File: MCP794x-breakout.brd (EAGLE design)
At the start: 22.8 x 15.2 mm, 11 parts, among them U4 MCP794x, X3 53261-02, Y2 ABS07

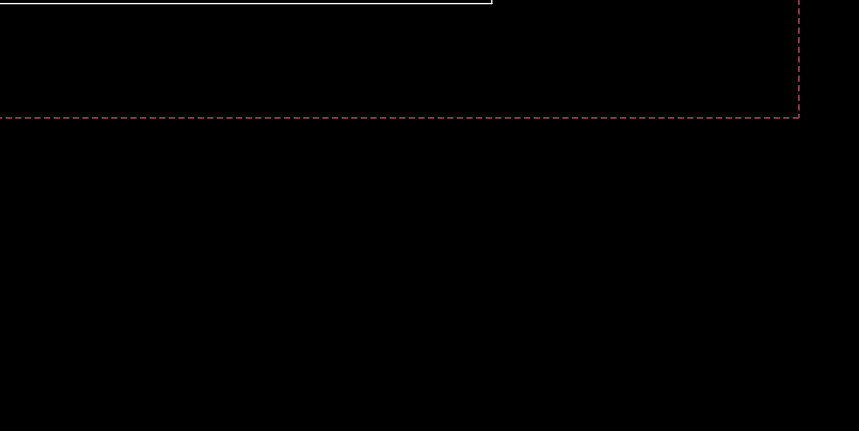
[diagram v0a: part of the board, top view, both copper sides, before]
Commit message: labels fixed
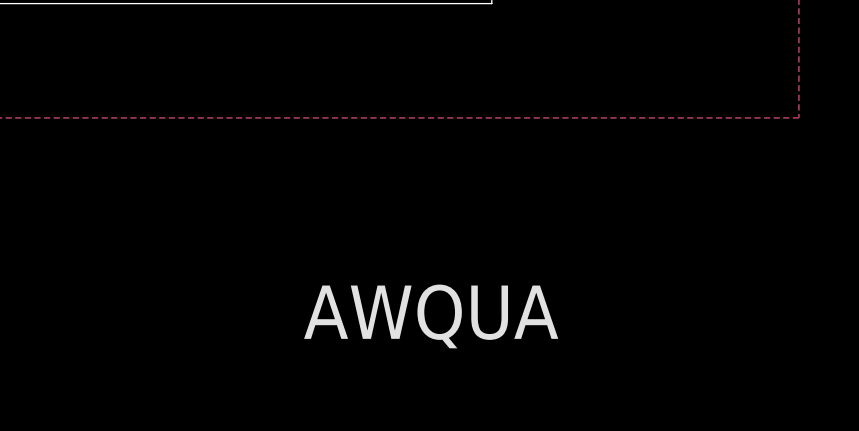
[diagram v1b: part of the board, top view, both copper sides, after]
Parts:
- moved FRAME1 84.2 mm to (-4.32, -10.9)
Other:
- board text added: "AWQUA"
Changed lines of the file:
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@@
 v1.0 2017-09-13
 CDK</text>
+<text x="16.51" y="-11.176" size="1.778" layer="25">AWQUA</text>
 </plain>
 <attributes>
@@
 <element name="C15" library="SparkFun-Passives" package="0603-CAP" value="100nF" x="12.7" y="2.794" rot="R270"/>
 <element name="C16" library="SparkFun-Passives" package="0603-CAP" value="100pF" x="16.256" y="9.906"/>
-<element name="FRAME1" library="SparkFun-Aesthetics" package="CREATIVE_COMMONS" value="FRAME-LETTER" x="-87.63" y="1.27"/>
+<element name="FRAME1" library="SparkFun-Aesthetics" package="CREATIVE_COMMONS" value="FRAME-LETTER" x="-4.318" y="-10.922"/>
 <element name="R12" library="SparkFun-Passives" package="0603-RES" value="1K" x="14.732" y="6.858" rot="R270"/>
 <element name="U$2" library="BAT43WS" package="BAT43WS" value="BAT43WS" x="16.256" y="3.556" smashed="yes">
